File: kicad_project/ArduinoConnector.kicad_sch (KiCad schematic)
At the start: 12 parts, among them J4 1x8, J5 1x8, J6 1x6, J7 1x10

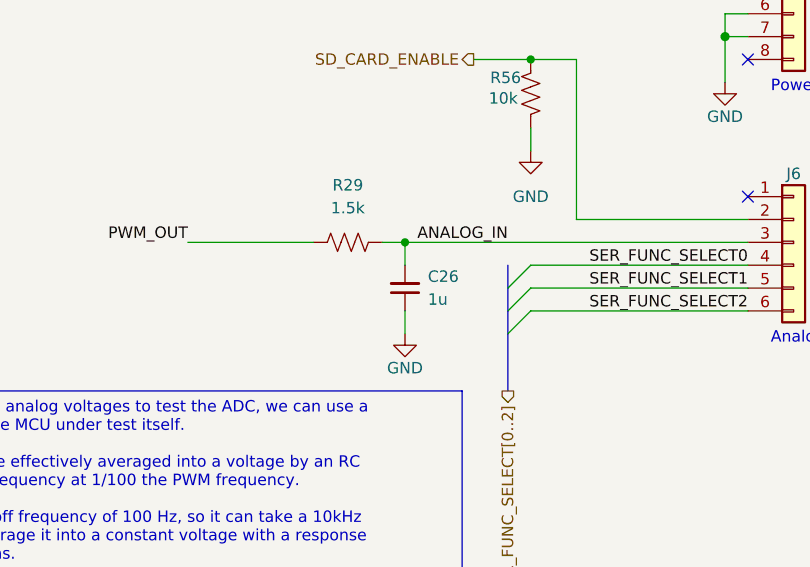
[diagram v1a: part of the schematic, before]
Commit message: Finish schematic and placement for all remaining RP2354 power passives
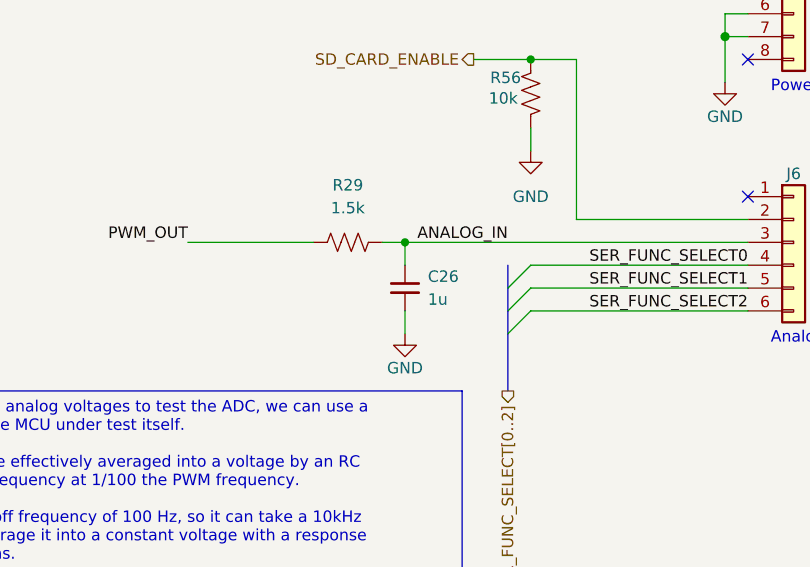
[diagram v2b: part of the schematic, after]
